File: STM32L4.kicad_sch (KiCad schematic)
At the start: 37 parts, among them J1 Conn_01x04_Pin, U5 MR20H40, U6 STM32L496RGTx, U7 TCAN334GDCNT, U8 TCAN334GDCNT, Y1 8 MHZ Oscillator

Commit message: LTC4162 layout almost done
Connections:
- net !GPIO_EN_OR_+X: no longer names the net of U6.26 (PB0)
- net !GPIO_EN_OR_+Y: no longer names the net of U6.59 (PB7)
- net !GPIO_EN_OR_-X: no longer names the net of U6.27 (PB1)
- net !GPIO_EN_OR_-Y: no longer names the net of U6.30 (PB11)
- net !GPIO_OR_GOOD_+X: no longer names the net of U6.37 (PC6)
- net !GPIO_OR_GOOD_+Y: no longer names the net of U6.42 (PA9)
- net !GPIO_OR_GOOD_-X: no longer names the net of U6.38 (PC7)
- net !GPIO_OR_GOOD_-Y: no longer names the net of U6.43 (PA10)

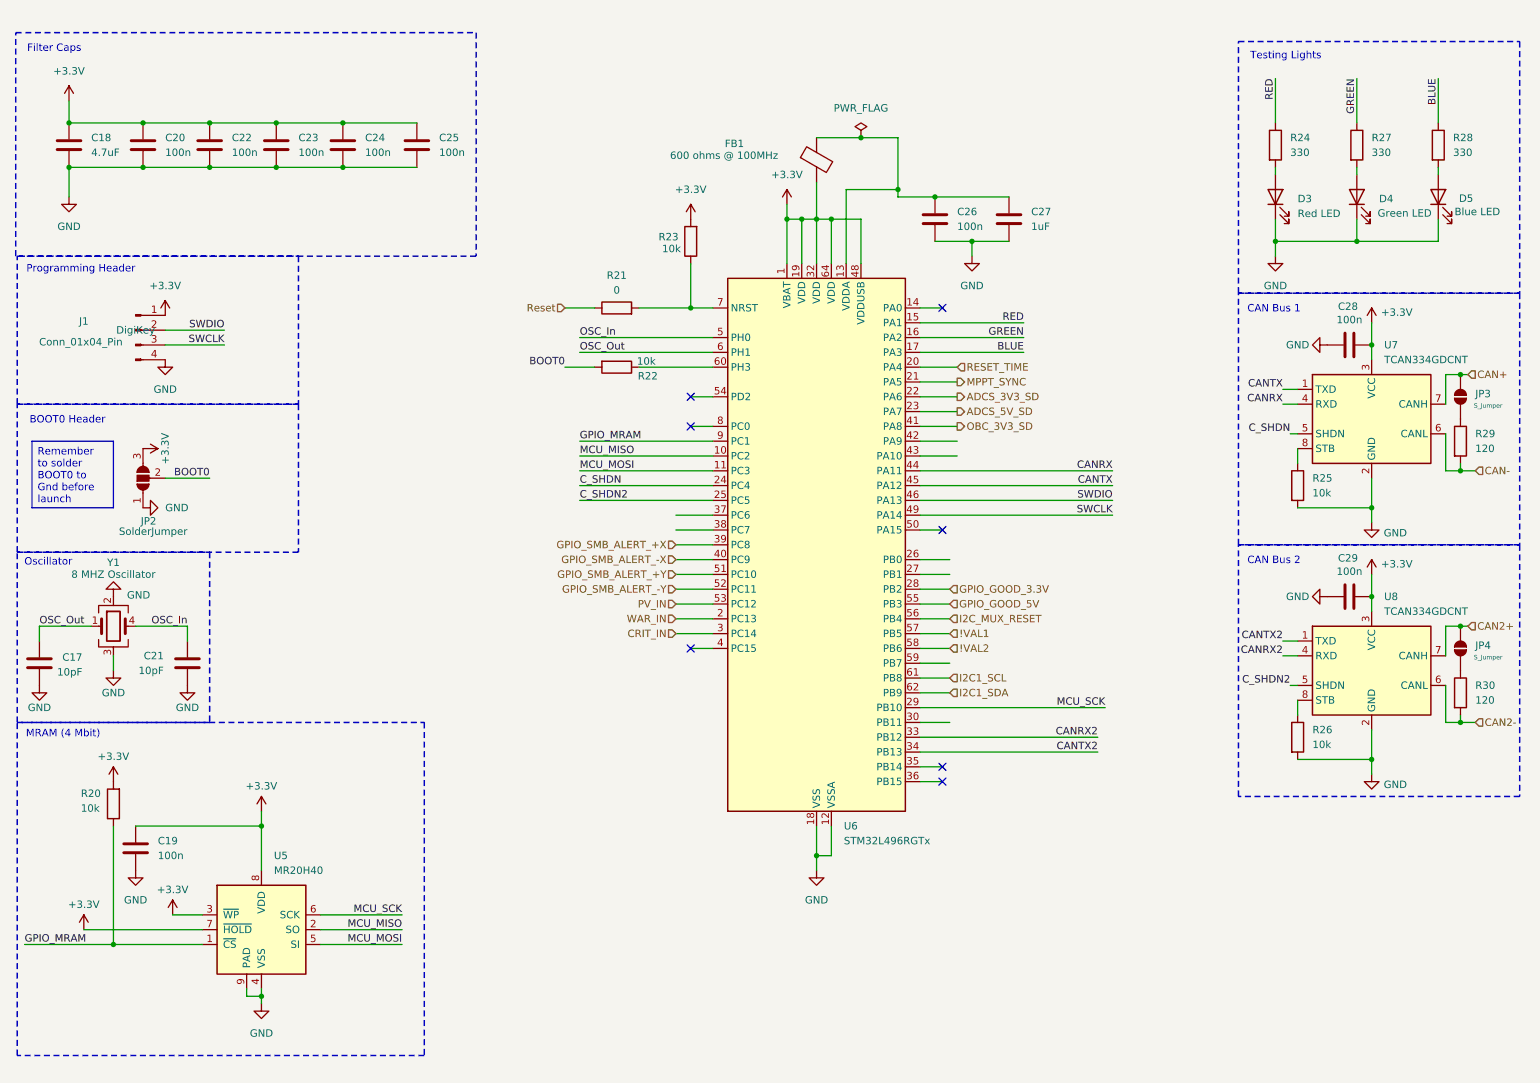
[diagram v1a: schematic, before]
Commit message: Efuses for this board and Battery board
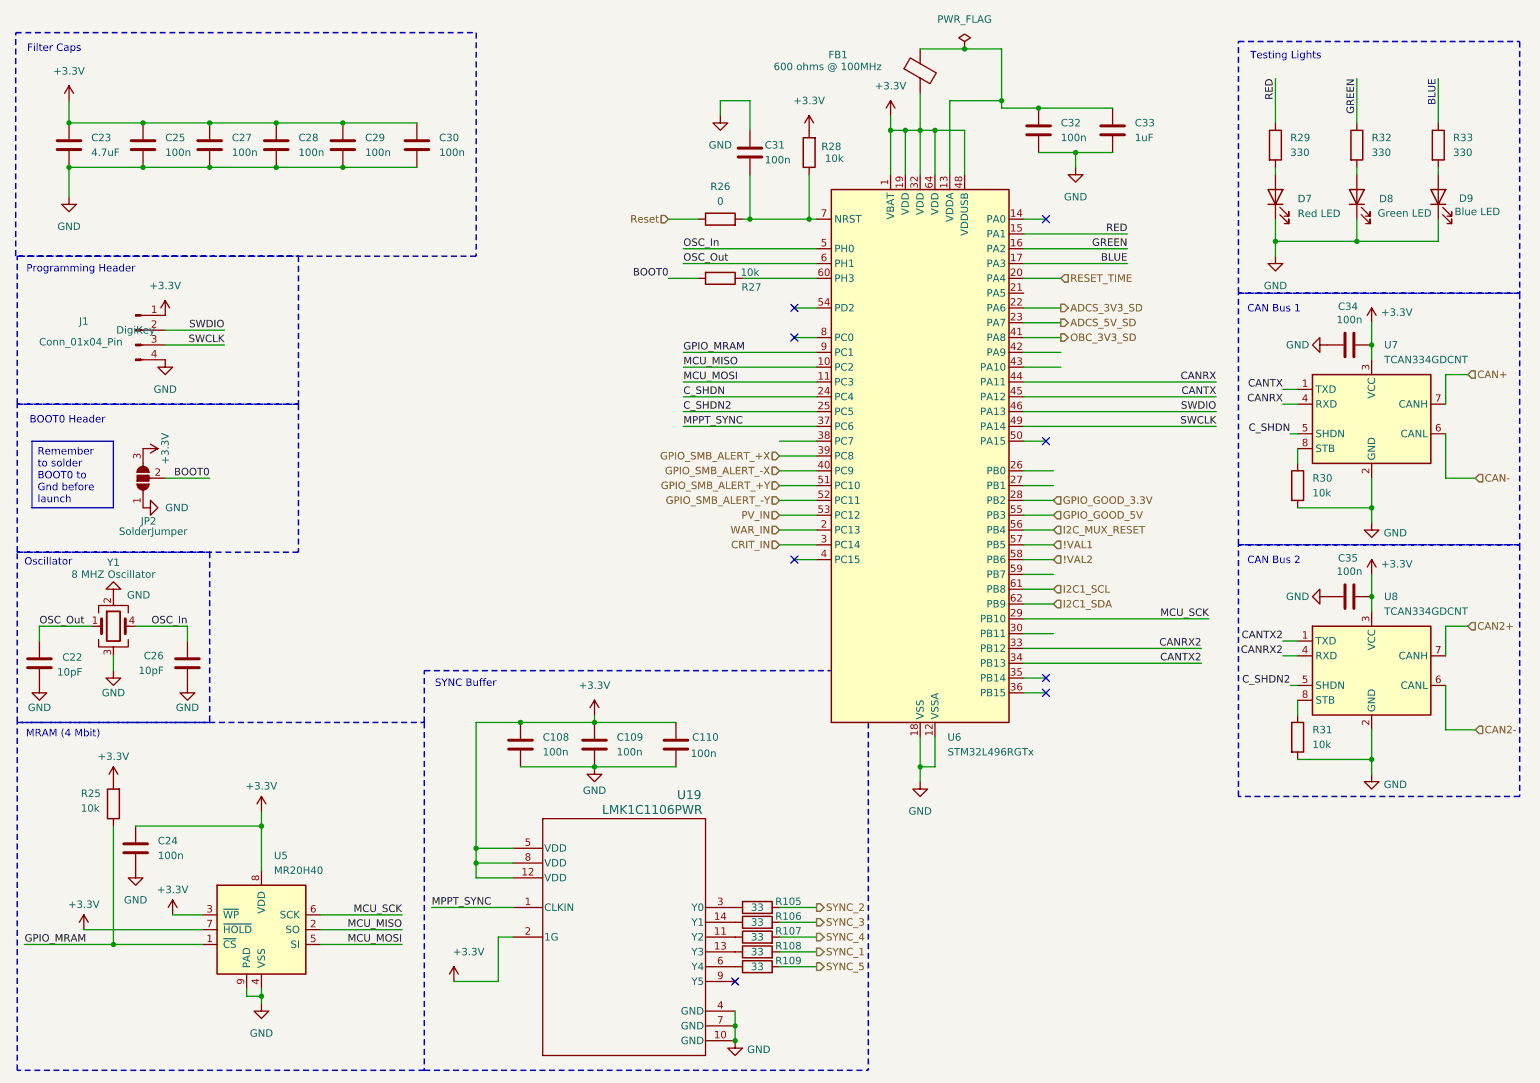
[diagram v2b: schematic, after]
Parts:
- removed JP3, JP4: S_Jumper, Jumper:SolderJumper-2_P1.3mm_Open_TrianglePad1.0x1.5mm, symbol Jumper:SolderJumper_2_Open
- removed R29, R30: 120, Resistor_SMD:R_0603_1608Metric, symbol Device:R
- added C108, C109, C110, C31: 100n, Capacitor_SMD:C_0603_1608Metric, symbol Device:C
- added R105, R106, R107, R108, R109: 33, Resistor_SMD:R_0402_1005Metric, symbol Device:R
- added U19: LMK1C1106PWR, zLibrary:PW0014A-IPC_B, symbol LMK1C1106PWR:LMK1C1106PWR
- renumbered C17 to C22, C18 to C23, C19 to C24, C20 to C25, C21 to C26, C22 to C27, C23 to C28, C24 to C29, C25 to C30, C26 to C32, C27 to C33, C28 to C34, C29 to C35, D3 to D7, D4 to D8, D5 to D9, R20 to R25, R21 to R26, R22 to R27, R23 to R28, R24 to R29, R25 to R30, R26 to R31, R27 to R32, R28 to R33
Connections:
- net +3.3V: now also C108.1, C109.1, C110.1, U19.12 (VDD), U19.2 (1G), U19.5 (VDD), U19.8 (VDD)
- net GND: now also C108.2, C109.2, C110.2, C31.1, U19.10 (GND), U19.4 (GND), U19.7 (GND)
- net MPPT_SYNC: now also U6.37 (PC6), U19.1 (CLKIN); no longer U6.21 (PA5)
- net at R26.2, R28.1, U6.7 (NRST): now also C31.2
- new net: R107.1, U19.11 (Y2)
- new net: R108.1, U19.13 (Y3)
- new net: R106.1, U19.14 (Y1)
- new net: R105.1, U19.3 (Y0)
- new net: R109.1, U19.6 (Y4)
- new net SYNC_1: R108.2
- new net SYNC_2: R105.2
- new net SYNC_3: R106.2
- new net SYNC_4: R107.2
- new net SYNC_5: R109.2
- no-connect marks 7 -> 8
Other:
- note added: "SYNC Buffer"
- moved on the sheet: C32, C33, FB1, R26, R27, R28, U6

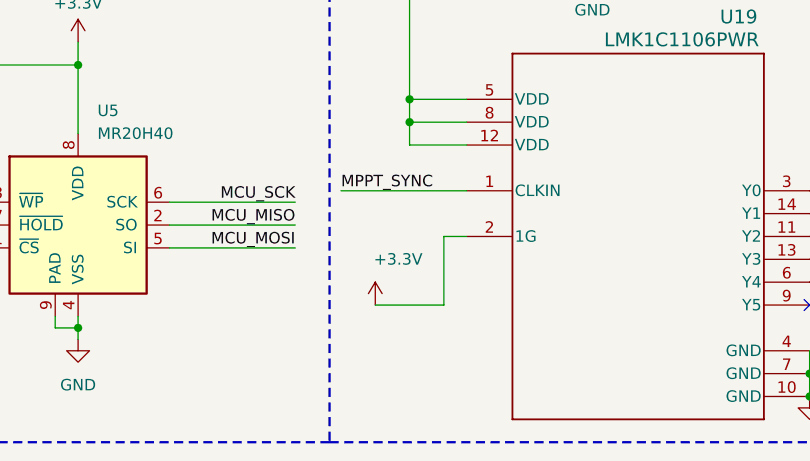
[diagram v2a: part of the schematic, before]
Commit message: Mostly done routing, still yet to start DRC
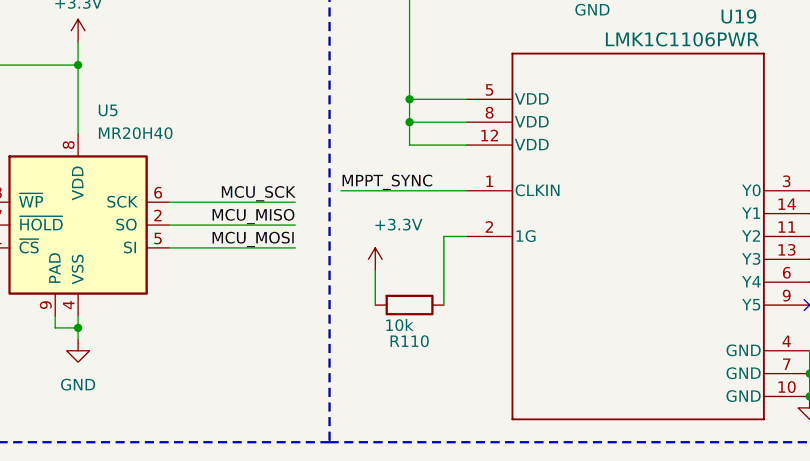
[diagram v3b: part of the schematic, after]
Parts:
- added R110: 10k, Resistor_SMD:R_0603_1608Metric, symbol Device:R
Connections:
- net +3.3V: now also R110.2; no longer U19.2 (1G)
- new net: R110.1, U19.2 (1G)
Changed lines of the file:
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@@
 	(wire
 		(pts
-			(xy 92.71 179.07) (xy 100.33 179.07)
-		)
-		(stroke
-			(width 0)
-			(type default)
-		)
-	)
-	(wire
-		(pts
 			(xy 132.08 76.2) (xy 154.94 76.2)
 		)
@@
 	(wire
 		(pts
+			(xy 92.71 175.26) (xy 92.71 179.07)
+		)
+		(stroke
+			(width 0)
+			(type default)
+		)
+	)
+	(wire
+		(pts
 			(xy 148.59 86.36) (xy 154.94 86.36)
 		)
@@
 	(symbol
 		(lib_id "power:+3.3V")
-		(at 92.71 179.07 0)
+		(at 92.71 175.26 0)
 		(unit 1)
 		(exclude_from_sim no)
@@
 		(dnp no)
 		(property "Reference" "#PWR0198"
-			(at 92.71 182.88 0)
+			(at 92.71 179.07 0)
 			(effects
 				(font
@@
 		)
 		(property "Value" "+3.3V"
-			(at 95.25 173.99 0)
+			(at 95.25 170.18 0)
 			(effects
 				(font
@@
 		)
 		(property "Footprint" ""
-			(at 92.71 179.07 0)
+			(at 92.71 175.26 0)
 			(effects
 				(font
@@
 		)
 		(property "Datasheet" ""
-			(at 92.71 179.07 0)
+			(at 92.71 175.26 0)
 			(effects
 				(font
@@
 		)
 		(property "Description" "Power symbol creates a global label with name \"+3.3V\""
-			(at 92.71 179.07 0)
+			(at 92.71 175.26 0)
 			(effects
 				(font
@@
 					(unit 1)
 				)
+			)
+		)
+	)
+	(symbol
+		(lib_id "Device:R")
+		(at 96.52 179.07 270)
+		(unit 1)
+		(exclude_from_sim no)
+		(in_bom yes)
+		(on_board yes)
+		(dnp no)
+		(property "Reference" "R110"
+			(at 94.234 183.134 90)
+			(effects
+				(font
+					(size 1.27 1.27)
+				)
+				(justify left)
+			)
+		)
+		(property "Value" "10k"
+			(at 93.726 181.356 90)
+			(effects
+				(font
+					(size 1.27 1.27)
+				)
+				(justify left)
+			)
+		)
+		(property "Footprint" "Resistor_SMD:R_0603_1608Metric"
+			(at 96.52 177.292 90)
+			(effects
+				(font
+					(size 1.27 1.27)
+				)
+				(hide yes)
+			)
+		)
+		(property "Datasheet" "~"
+			(at 96.52 179.07 0)
+			(effects
+				(font
+					(size 1.27 1.27)
+				)
+				(hide yes)
+			)
+		)
+		(property "Description" "Resistor"
+			(at 96.52 179.07 0)
+			(effects
+				(font
+					(size 1.27 1.27)
+				)
+				(hide yes)
+			)
+		)
+		(property "MANUFACTURER_PART_NUMBER" ""
+			(at 96.52 179.07 0)
+			(effects
+				(font
+					(size 1.27 1.27)
+				)
+				(hide yes)
+			)
+		)
+		(property "MANUFACTURER" "Digikey"
+			(at 96.52 179.07 0)
+			(effects
+				(font
+					(size 1.27 1.27)
+				)
+				(hide yes)
+			)
+		)
+		(property "Sim.Device" ""
+			(at 96.52 179.07 0)
+			(effects
+				(font
+					(size 1.27 1.27)
+				)
+			)
+		)
+		(property "Sim.Type" ""
+			(at 96.52 179.07 0)
+			(effects
+				(font
+					(size 1.27 1.27)
+				)
+			)
+		)
+		(pin "1"
+		)
+		(pin "2"
+		)
+		(instances
+			(project "EPS_mppt_board"
+				(path "/8f246f89-1ec7-4136-9977-839b50e116ed/bc2f1682-e3ae-4ffc-84d8-70ef19ac3f89"
+					(reference "R110")
+					(unit 1)
+				)
